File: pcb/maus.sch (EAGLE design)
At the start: 89 parts, among them J1 SS-52300-001, Q1 BSS123, Q2 BSS123, Q3 BSS123, Q4 BSS123, Q5 BSS123, Q6 SI3499DV-T1-BE3, Q7 SI3499DV-T1-BE3, U1 ESP32-S2-WROOM, U2 CH340C, U3 CP2102, U4 LP3965EMP-3.3, U5 LSM9DS1TR, U6 LM358DR

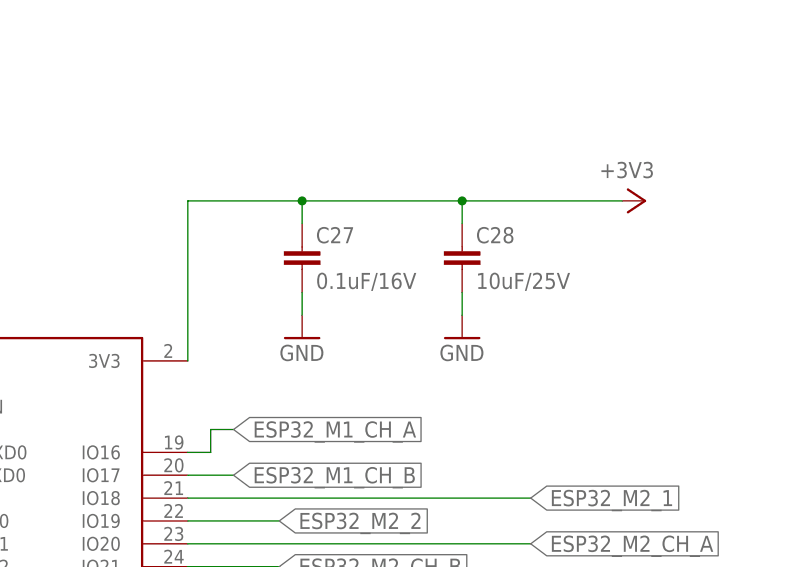
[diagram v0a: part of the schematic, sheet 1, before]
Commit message: fix: remove extra caps from 3v3 esp32
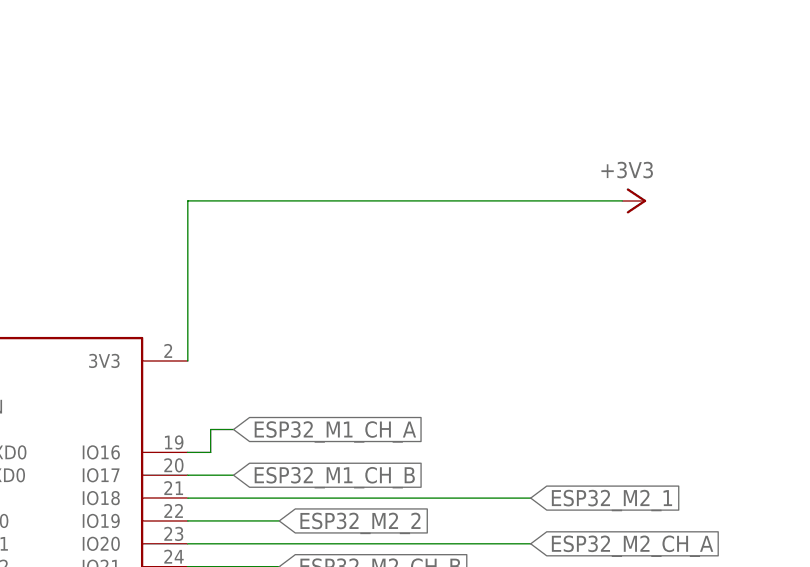
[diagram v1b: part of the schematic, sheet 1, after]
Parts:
- removed C27: 0.1uF/16V, rcl:C-EUC0805
- removed C28: 10uF/25V, rcl:C-EUC0805
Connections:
- net +3V3: no longer C27.1, C28.1
- net GND: no longer C27.2, C28.2
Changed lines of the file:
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@@
 <part name="R20" library="rcl" library_urn="urn:adsk.eagle:library:334" deviceset="R-EU_" device="R0805" package3d_urn="urn:adsk.eagle:package:23553/2" value="1k"/>
 <part name="D5" library="SparkFun-LED" library_urn="urn:adsk.eagle:library:529" deviceset="LED-RED" device="1206" value="RED"/>
-<part name="C27" library="rcl" library_urn="urn:adsk.eagle:library:334" deviceset="C-EU" device="C0805" package3d_urn="urn:adsk.eagle:package:23617/2" value="0.1uF/16V"/>
-<part name="C28" library="rcl" library_urn="urn:adsk.eagle:library:334" deviceset="C-EU" device="C0805" package3d_urn="urn:adsk.eagle:package:23617/2" value="10uF/25V"/>
-<part name="GND36" library="supply1" library_urn="urn:adsk.eagle:library:371" deviceset="GND" device=""/>
-<part name="GND37" library="supply1" library_urn="urn:adsk.eagle:library:371" deviceset="GND" device=""/>
 <part name="SV2" library="con-harting-ml" library_urn="urn:adsk.eagle:library:149" deviceset="ML6" device="" package3d_urn="urn:adsk.eagle:package:6988/1"/>
 <part name="GND35" library="supply1" library_urn="urn:adsk.eagle:library:371" deviceset="GND" device=""/>
@@
 <attribute name="VALUE" x="50.165" y="173.228" size="1.778" layer="96" font="vector" rot="R90" align="top-left"/>
 </instance>
-<instance part="C27" gate="G$1" x="129.54" y="106.68" smashed="yes">
-<attribute name="NAME" x="131.064" y="107.061" size="1.778" layer="95"/>
-<attribute name="VALUE" x="131.064" y="101.981" size="1.778" layer="96"/>
-</instance>
-<instance part="C28" gate="G$1" x="147.32" y="106.68" smashed="yes">
-<attribute name="NAME" x="148.844" y="107.061" size="1.778" layer="95"/>
-<attribute name="VALUE" x="148.844" y="101.981" size="1.778" layer="96"/>
-</instance>
-<instance part="GND36" gate="1" x="129.54" y="96.52" smashed="yes">
-<attribute name="VALUE" x="127" y="93.98" size="1.778" layer="96"/>
-</instance>
-<instance part="GND37" gate="1" x="147.32" y="96.52" smashed="yes">
-<attribute name="VALUE" x="144.78" y="93.98" size="1.778" layer="96"/>
-</instance>
 <instance part="R23" gate="G$1" x="88.9" y="190.5" smashed="yes" rot="R90">
 <attribute name="NAME" x="87.4014" y="186.69" size="1.778" layer="95" rot="R90"/>
@@
 <pinref part="U1" gate="G$1" pin="3V3"/>
 <wire x1="116.84" y1="93.98" x2="116.84" y2="111.76" width="0.1524" layer="91"/>
-<wire x1="116.84" y1="111.76" x2="129.54" y2="111.76" width="0.1524" layer="91"/>
 <pinref part="+3V6" gate="G$1" pin="+3V3"/>
-<wire x1="129.54" y1="111.76" x2="147.32" y2="111.76" width="0.1524" layer="91"/>
-<wire x1="147.32" y1="111.76" x2="165.1" y2="111.76" width="0.1524" layer="91"/>
-<wire x1="129.54" y1="111.76" x2="129.54" y2="109.22" width="0.1524" layer="91"/>
-<junction x="129.54" y="111.76"/>
-<pinref part="C27" gate="G$1" pin="1"/>
-<pinref part="C28" gate="G$1" pin="1"/>
-<wire x1="147.32" y1="111.76" x2="147.32" y2="109.22" width="0.1524" layer="91"/>
-<junction x="147.32" y="111.76"/>
+<wire x1="116.84" y1="111.76" x2="165.1" y2="111.76" width="0.1524" layer="91"/>
 </segment>
 <segment>
@@
 </segment>
 <segment>
-<pinref part="GND36" gate="1" pin="GND"/>
-<pinref part="C27" gate="G$1" pin="2"/>
-<wire x1="129.54" y1="99.06" x2="129.54" y2="101.6" width="0.1524" layer="91"/>
-</segment>
-<segment>
-<pinref part="GND37" gate="1" pin="GND"/>
-<pinref part="C28" gate="G$1" pin="2"/>
-<wire x1="147.32" y1="99.06" x2="147.32" y2="101.6" width="0.1524" layer="91"/>
-</segment>
-<segment>

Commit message: Revert "fix: remove extra caps from 3v3 esp32"
This reverts commit 98a652b0698d76106b42ebf40b6ec01f9ce7920d.
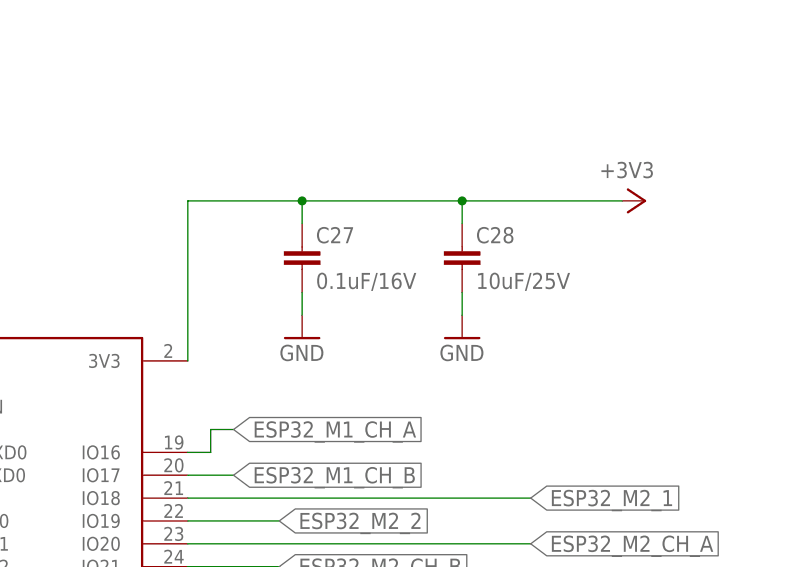
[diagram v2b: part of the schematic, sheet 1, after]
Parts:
- added C27: 0.1uF/16V, rcl:C-EUC0805
- added C28: 10uF/25V, rcl:C-EUC0805
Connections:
- net +3V3: now also C27.1, C28.1
- net GND: now also C27.2, C28.2
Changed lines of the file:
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@@
 <part name="R20" library="rcl" library_urn="urn:adsk.eagle:library:334" deviceset="R-EU_" device="R0805" package3d_urn="urn:adsk.eagle:package:23553/2" value="1k"/>
 <part name="D5" library="SparkFun-LED" library_urn="urn:adsk.eagle:library:529" deviceset="LED-RED" device="1206" value="RED"/>
+<part name="C27" library="rcl" library_urn="urn:adsk.eagle:library:334" deviceset="C-EU" device="C0805" package3d_urn="urn:adsk.eagle:package:23617/2" value="0.1uF/16V"/>
+<part name="C28" library="rcl" library_urn="urn:adsk.eagle:library:334" deviceset="C-EU" device="C0805" package3d_urn="urn:adsk.eagle:package:23617/2" value="10uF/25V"/>
+<part name="GND36" library="supply1" library_urn="urn:adsk.eagle:library:371" deviceset="GND" device=""/>
+<part name="GND37" library="supply1" library_urn="urn:adsk.eagle:library:371" deviceset="GND" device=""/>
 <part name="SV2" library="con-harting-ml" library_urn="urn:adsk.eagle:library:149" deviceset="ML6" device="" package3d_urn="urn:adsk.eagle:package:6988/1"/>
 <part name="GND35" library="supply1" library_urn="urn:adsk.eagle:library:371" deviceset="GND" device=""/>
@@
 <attribute name="VALUE" x="50.165" y="173.228" size="1.778" layer="96" font="vector" rot="R90" align="top-left"/>
 </instance>
+<instance part="C27" gate="G$1" x="129.54" y="106.68" smashed="yes">
+<attribute name="NAME" x="131.064" y="107.061" size="1.778" layer="95"/>
+<attribute name="VALUE" x="131.064" y="101.981" size="1.778" layer="96"/>
+</instance>
+<instance part="C28" gate="G$1" x="147.32" y="106.68" smashed="yes">
+<attribute name="NAME" x="148.844" y="107.061" size="1.778" layer="95"/>
+<attribute name="VALUE" x="148.844" y="101.981" size="1.778" layer="96"/>
+</instance>
+<instance part="GND36" gate="1" x="129.54" y="96.52" smashed="yes">
+<attribute name="VALUE" x="127" y="93.98" size="1.778" layer="96"/>
+</instance>
+<instance part="GND37" gate="1" x="147.32" y="96.52" smashed="yes">
+<attribute name="VALUE" x="144.78" y="93.98" size="1.778" layer="96"/>
+</instance>
 <instance part="R23" gate="G$1" x="88.9" y="190.5" smashed="yes" rot="R90">
 <attribute name="NAME" x="87.4014" y="186.69" size="1.778" layer="95" rot="R90"/>
@@
 <pinref part="U1" gate="G$1" pin="3V3"/>
 <wire x1="116.84" y1="93.98" x2="116.84" y2="111.76" width="0.1524" layer="91"/>
+<wire x1="116.84" y1="111.76" x2="129.54" y2="111.76" width="0.1524" layer="91"/>
 <pinref part="+3V6" gate="G$1" pin="+3V3"/>
-<wire x1="116.84" y1="111.76" x2="165.1" y2="111.76" width="0.1524" layer="91"/>
+<wire x1="129.54" y1="111.76" x2="147.32" y2="111.76" width="0.1524" layer="91"/>
+<wire x1="147.32" y1="111.76" x2="165.1" y2="111.76" width="0.1524" layer="91"/>
+<wire x1="129.54" y1="111.76" x2="129.54" y2="109.22" width="0.1524" layer="91"/>
+<junction x="129.54" y="111.76"/>
+<pinref part="C27" gate="G$1" pin="1"/>
+<pinref part="C28" gate="G$1" pin="1"/>
+<wire x1="147.32" y1="111.76" x2="147.32" y2="109.22" width="0.1524" layer="91"/>
+<junction x="147.32" y="111.76"/>
 </segment>
 <segment>
@@
 </segment>
 <segment>
+<pinref part="GND36" gate="1" pin="GND"/>
+<pinref part="C27" gate="G$1" pin="2"/>
+<wire x1="129.54" y1="99.06" x2="129.54" y2="101.6" width="0.1524" layer="91"/>
+</segment>
+<segment>
+<pinref part="GND37" gate="1" pin="GND"/>
+<pinref part="C28" gate="G$1" pin="2"/>
+<wire x1="147.32" y1="99.06" x2="147.32" y2="101.6" width="0.1524" layer="91"/>
+</segment>
+<segment>

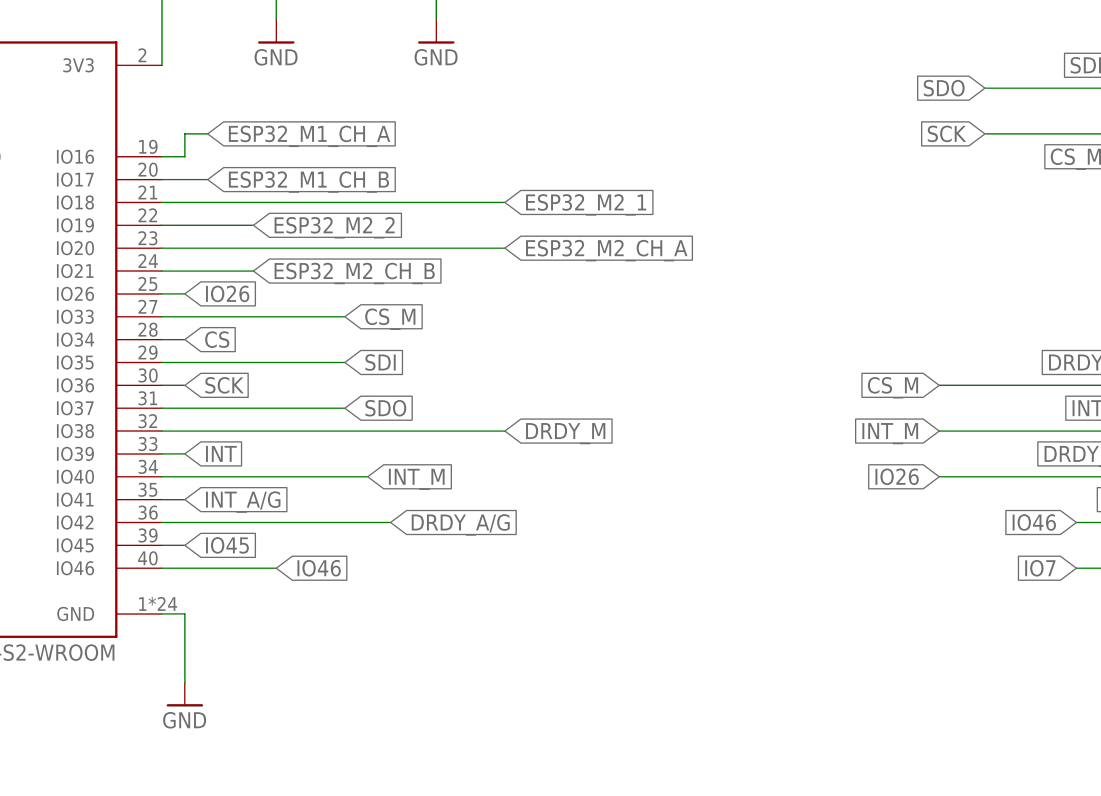
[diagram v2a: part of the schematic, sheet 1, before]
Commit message: moved modor 2 pins and added pullup to io18
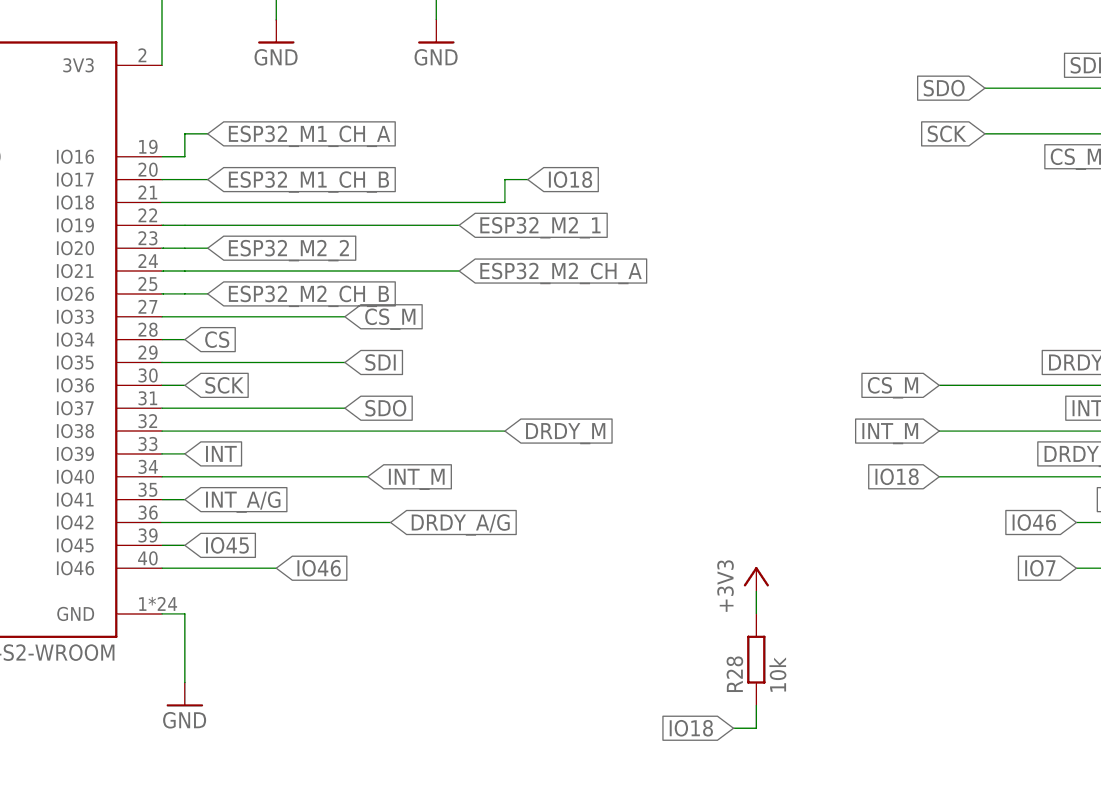
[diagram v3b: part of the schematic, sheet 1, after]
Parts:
- added R28: 10k, rcl:R-EU_R0805
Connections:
- removed net IO26: JP5.6, U1.IO26
- new net IO18: JP5.6, R28.1, U1.IO18
- net +3V3: now also R28.2
- net ESP32_M2_1: now also U1.IO19; no longer U1.IO18
- net ESP32_M2_2: now also U1.IO20; no longer U1.IO19
- net ESP32_M2_CH_A: now also U1.IO21; no longer U1.IO20
- net ESP32_M2_CH_B: now also U1.IO26; no longer U1.IO21
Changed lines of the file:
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@@
 <drawing>
 <settings>
-<setting alwaysvectorfont="yes"/>
+<setting alwaysvectorfont="no"/>
 <setting verticaltext="up"/>
 </settings>
@@
 <part name="GND43" library="supply1" library_urn="urn:adsk.eagle:library:371" deviceset="GND" device=""/>
 <part name="J1" library="shared" deviceset="SS-52300-001" device=""/>
+<part name="R28" library="rcl" library_urn="urn:adsk.eagle:library:334" deviceset="R-EU_" device="R0805" package3d_urn="urn:adsk.eagle:package:23553/2" value="10k"/>
+<part name="+3V15" library="supply1" library_urn="urn:adsk.eagle:library:371" deviceset="+3V3" device=""/>
 </parts>
 <sheets>
@@
 <attribute name="VALUE" x="223.52" y="76.2" size="1.778" layer="96"/>
 </instance>
+<instance part="R28" gate="G$1" x="182.88" y="27.94" smashed="yes" rot="R90">
+<attribute name="NAME" x="181.3814" y="24.13" size="1.778" layer="95" rot="R90"/>
+<attribute name="VALUE" x="186.182" y="24.13" size="1.778" layer="96" rot="R90"/>
+</instance>
+<instance part="+3V15" gate="G$1" x="182.88" y="38.1" smashed="yes">
+<attribute name="VALUE" x="180.34" y="33.02" size="1.778" layer="96" rot="R90"/>
+</instance>
 </instances>
 <busses>
@@
 <wire x1="139.7" y1="198.12" x2="139.7" y2="195.58" width="0.1524" layer="91"/>
 <pinref part="+3V12" gate="G$1" pin="+3V3"/>
+</segment>
+<segment>
+<pinref part="+3V15" gate="G$1" pin="+3V3"/>
+<pinref part="R28" gate="G$1" pin="2"/>
+<wire x1="182.88" y1="35.56" x2="182.88" y2="33.02" width="0.1524" layer="91"/>
 </segment>
 </net>
@@
 <net name="ESP32_M2_1" class="0">
 <segment>
-<pinref part="U1" gate="G$1" pin="IO18"/>
-<wire x1="116.84" y1="78.74" x2="154.94" y2="78.74" width="0.1524" layer="91"/>
-<label x="154.94" y="78.74" size="1.778" layer="95" xref="yes"/>
+<label x="149.86" y="76.2" size="1.778" layer="95" xref="yes"/>
+<wire x1="116.9924" y1="76.2" x2="119.38" y2="76.2" width="0.1524" layer="91"/>
+<pinref part="U1" gate="G$1" pin="IO19"/>
+<wire x1="119.38" y1="76.2" x2="149.86" y2="76.2" width="0.1524" layer="91"/>
+<wire x1="116.84" y1="76.2" x2="116.9924" y2="76.2" width="0.1524" layer="91"/>
 </segment>
 </net>
 <net name="ESP32_M2_2" class="0">
 <segment>
-<pinref part="U1" gate="G$1" pin="IO19"/>
-<wire x1="116.84" y1="76.2" x2="127" y2="76.2" width="0.1524" layer="91"/>
-<label x="127" y="76.2" size="1.778" layer="95" xref="yes"/>
+<label x="121.92" y="73.66" size="1.778" layer="95" xref="yes"/>
+<wire x1="116.9924" y1="73.66" x2="119.38" y2="73.66" width="0.1524" layer="91"/>
+<pinref part="U1" gate="G$1" pin="IO20"/>
+<wire x1="119.38" y1="73.66" x2="121.92" y2="73.66" width="0.1524" layer="91"/>
+<wire x1="116.84" y1="73.66" x2="116.9924" y2="73.66" width="0.1524" layer="91"/>
 </segment>
 </net>
 <net name="ESP32_M2_CH_A" class="0">
 <segment>
-<pinref part="U1" gate="G$1" pin="IO20"/>
-<wire x1="116.84" y1="73.66" x2="154.94" y2="73.66" width="0.1524" layer="91"/>
-<label x="154.94" y="73.66" size="1.778" layer="95" xref="yes"/>
+<label x="149.86" y="71.12" size="1.778" layer="95" xref="yes"/>
+<wire x1="116.9924" y1="71.12" x2="119.38" y2="71.12" width="0.1524" layer="91"/>
+<pinref part="U1" gate="G$1" pin="IO21"/>
+<wire x1="119.38" y1="71.12" x2="149.86" y2="71.12" width="0.1524" layer="91"/>
+<wire x1="116.84" y1="71.12" x2="116.9924" y2="71.12" width="0.1524" layer="91"/>
 </segment>
 </net>
 <net name="ESP32_M2_CH_B" class="0">
 <segment>
-<pinref part="U1" gate="G$1" pin="IO21"/>
-<wire x1="116.84" y1="71.12" x2="127" y2="71.12" width="0.1524" layer="91"/>
-<label x="127" y="71.12" size="1.778" layer="95" xref="yes"/>
+<label x="121.92" y="68.58" size="1.778" layer="95" xref="yes"/>
+<wire x1="116.9924" y1="68.58" x2="119.38" y2="68.58" width="0.1524" layer="91"/>
+<pinref part="U1" gate="G$1" pin="IO26"/>
+<wire x1="119.38" y1="68.58" x2="121.92" y2="68.58" width="0.1524" layer="91"/>
+<wire x1="116.84" y1="68.58" x2="116.9924" y2="68.58" width="0.1524" layer="91"/>
 </segment>
 </net>
@@
 </segment>
 </net>
-<net name="IO26" class="0">
+<net name="IO18" class="0">
 <segment>
 <pinref part="JP5" gate="A" pin="6"/>
@@
 </segment>
 <segment>
-<pinref part="U1" gate="G$1" pin="IO26"/>
-<wire x1="116.84" y1="68.58" x2="119.38" y2="68.58" width="0.1524" layer="91"/>
-<label x="119.38" y="68.58" size="1.778" layer="95" xref="yes"/>
-</segment>
-</net>
+<pinref part="U1" gate="G$1" pin="IO18"/>
+<wire x1="116.84" y1="78.74" x2="154.94" y2="78.74" width="0.1524" layer="91"/>
+<wire x1="154.94" y1="78.74" x2="154.94" y2="81.28" width="0.1524" layer="91"/>
+<wire x1="154.94" y1="81.28" x2="157.48" y2="81.28" width="0.1524" layer="91"/>
+<label x="157.48" y="81.28" size="1.778" layer="95" xref="yes"/>
+</segment>
+<segment>
+<pinref part="R28" gate="G$1" pin="1"/>
+<wire x1="182.88" y1="22.86" x2="182.88" y2="20.32" width="0.1524" layer="91"/>
+<wire x1="182.88" y1="20.32" x2="180.34" y2="20.32" width="0.1524" layer="91"/>
+<label x="180.34" y="20.32" size="1.778" layer="95" rot="R180" xref="yes"/>
+</segment>
+</net>
